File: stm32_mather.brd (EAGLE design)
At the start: 100 x 80 mm, 56 parts

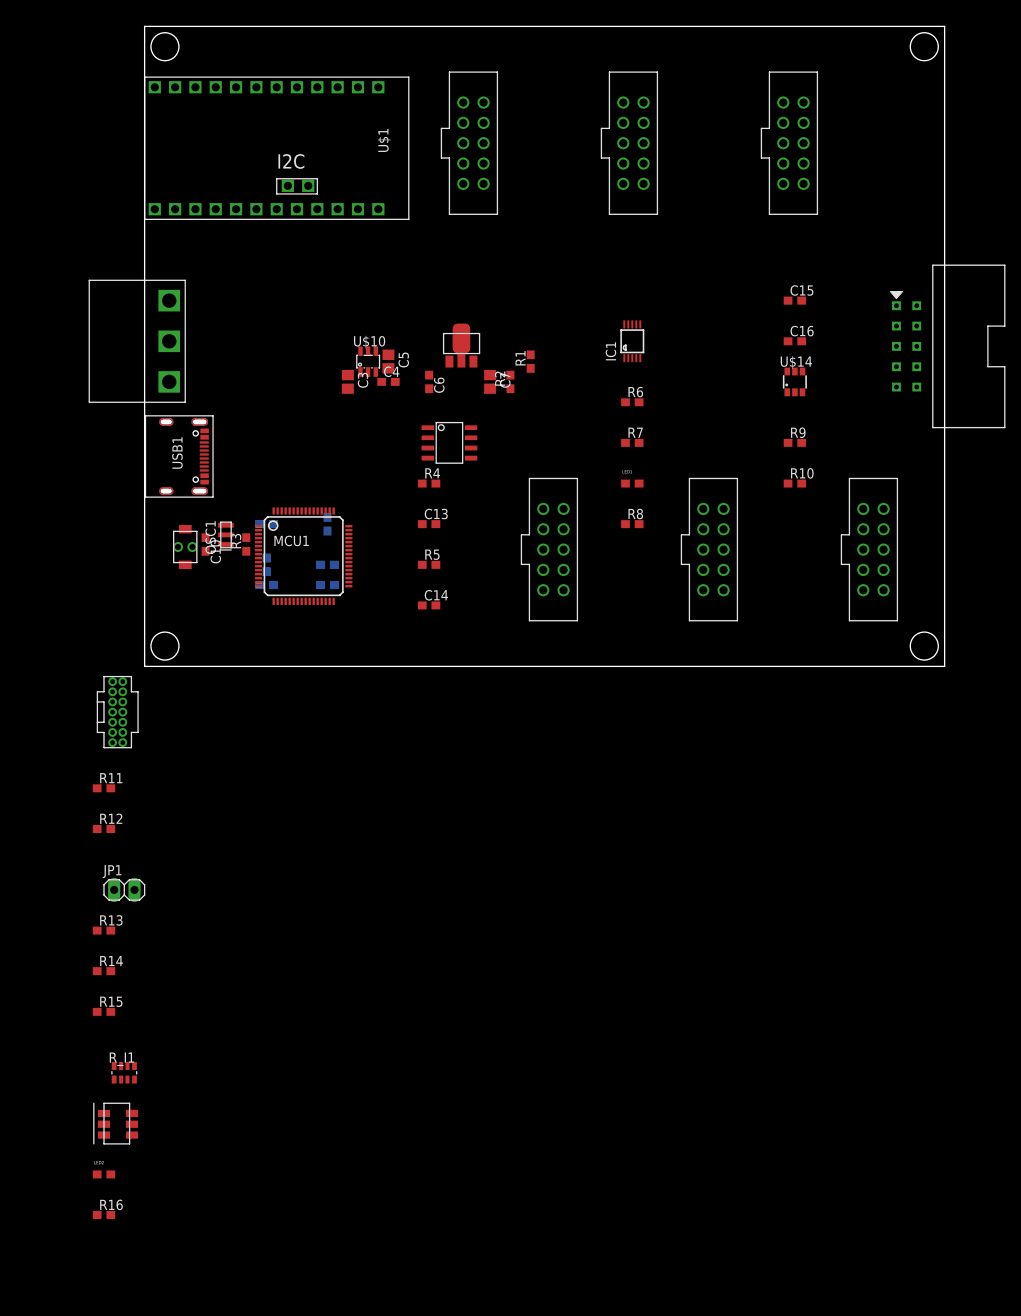
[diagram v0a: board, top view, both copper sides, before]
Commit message: デバッガを組み込む方式に変更 3.3vのリニアレギュレータを単純化
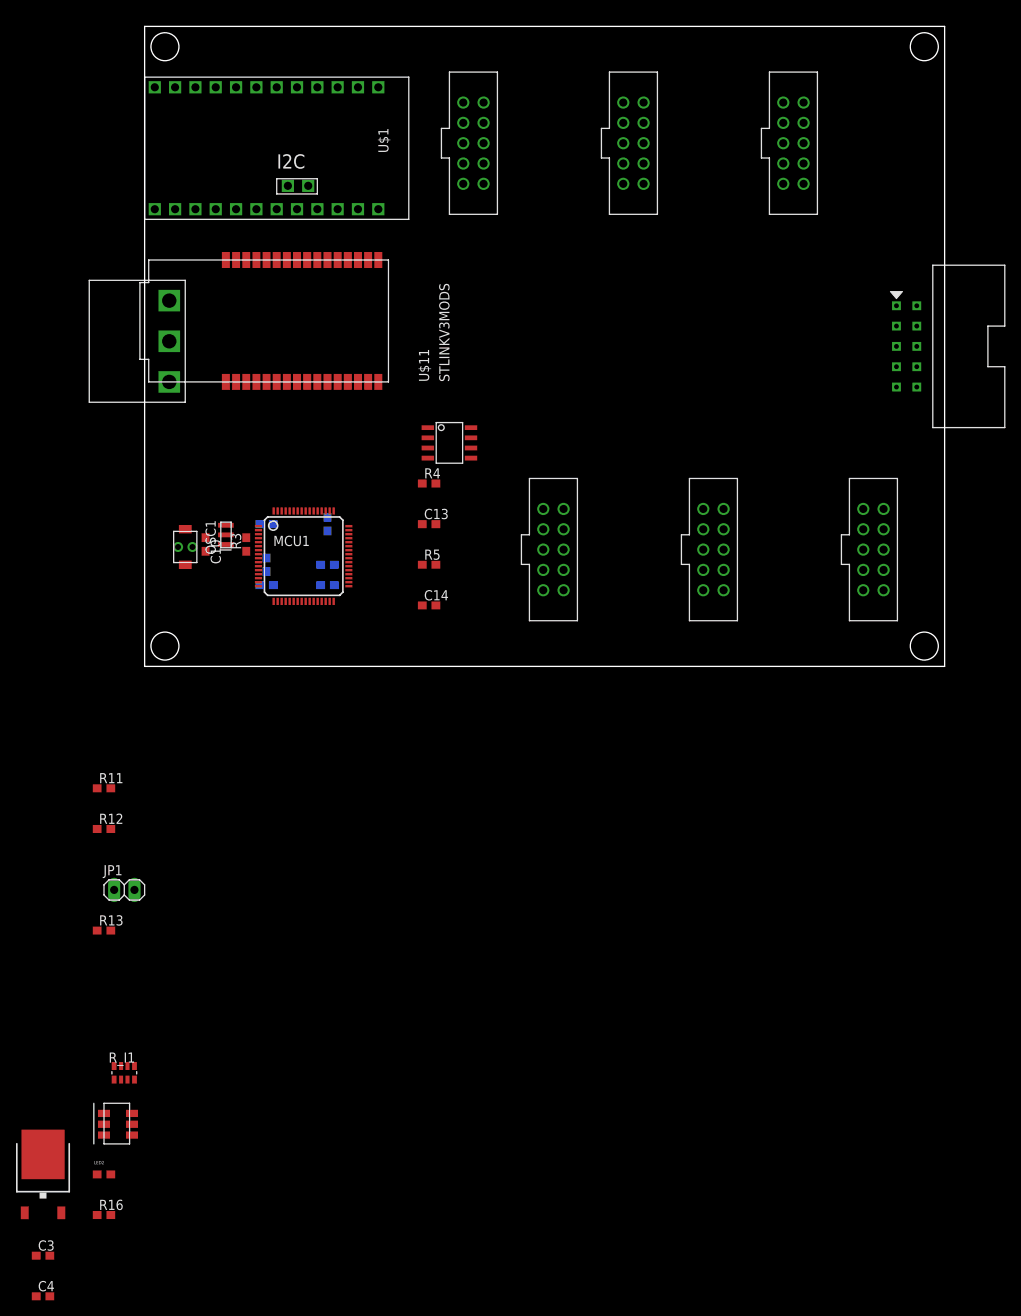
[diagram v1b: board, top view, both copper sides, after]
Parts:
- removed C15: 0.1u, rcl:C1608
- removed C16: (no value), rcl:C1608
- removed C5: 4.7u, rcl:C2012
- removed C6: 470p, rcl:C1608
- removed C7: 10u, rcl:C2012
- removed IC1: (no value), user_ic:MSOP10
- removed LED1: (no value), user_leds:1608
- removed R1: 33k, user_rcl:1608
- removed R10, R14, R15, R9: 10k, user_rcl:1608
- removed R2: 20k, user_rcl:1608
- removed R6, R7: 5.1k, user_rcl:1608
- removed R8: 1k, user_rcl:1608
- removed U$14: FDC6305, user_tr_fet_igbt:SSOT6
- removed U$22: BOX14P, user_conector:CON_HEDA14P_1.27
- removed USB1: (no value), user_conector:USB_TYPE_C
- C3: value 0.22u -> 1u; device rcl:C2012 -> rcl:C1608
- C4: value 0.1u -> 2.2u
- U$10: value NJM11100 -> NJM2845; device user_ic:SOT23-6 -> user_ic:TO252
- U$11: value 2SC5964 -> STLINKV3MODS; device user_tr_fet_igbt:PCP -> user_ic:STLINKV3MODS
- moved C4 122.2 mm to (-12.7, -78.7)
- moved C3 115.7 mm to (-12.7, -73.7), turned to 0 degrees
- moved U$10 109.4 mm to (-12.7, -63.5)
- moved U$11 8.03 mm to (30.5, 35.6), turned to 90 degrees
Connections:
- removed net N$1: C6.2, R1.1, R2.2, U$10.5
- removed net N$17: IC1.1, USB1.A6, USB1.B6
- removed net N$18: IC1.2, USB1.A7, USB1.B7
- removed net N$2: C4.1, U$10.3
- removed net N$20: R7.2, USB1.A5
- removed net N$21: R6.2, USB1.B5
- removed net N$22: IC1.6, R8.1
- removed net N$23: LED1.A, R8.2
- removed net N$24: C15.1, IC1.10
- removed net N$25: IC1.4, IC1.5
- removed net N$26: IC1.8, R10.2, U$14.2
- removed net N$28: IC1.9, R9.1, U$14.5
- removed net N$3: C5.1, C6.1, U$10.4, U$11.1
- removed net USART1_RX: MCU1.59, R14.1, U$14.4
- removed net USART1_TX: MCU1.58, R15.1, U$14.6
- net GND: now also U$10.PIN2, U$11.24, U$11.26, U$11.27, U$11.29, U$11.5, U$11.8; no longer C15.2, C16.2, C5.2, C7.2, IC1.3, LED1.K, R2.1, R6.1, R7.1, U$10.2, U$22.11, U$22.5, U$22.7, USB1.A1_B12, USB1.B1_A12
- net JTCK: now also U$11.13; no longer U$22.6
- net JTDI: now also U$11.28; no longer U$22.10
- net JTDO: now also U$11.6; no longer U$22.8
- net JTMS: now also U$11.4; no longer U$22.4
- net NRST: now also U$11.31; no longer U$22.12
- net RX: now also U$11.15; no longer U$22.13
- net TX: now also U$11.12; no longer U$22.14
- net V3.3: now also C4.1, U$10.PIN3, U$11.30; no longer C7.1, R1.2, R14.2, R15.2, U$11.3, U$22.3
- net V5: now also U$10.PIN1; no longer C16.1, IC1.7, R10.1, R9.2, U$10.1, U$10.6, U$11.2, U$11.2@2, U$14.1, U$14.3, USB1.A4_B9, USB1.B4_A9

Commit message: 基板図の設計完了
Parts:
- R_I1: value (none) -> 1k
- moved C4 119.6 mm to (11.8, 38.3), turned to 270 degrees
- moved R16 118.6 mm to (29.5, 44.8)
- moved R13 115.2 mm to (83.7, 40.4), flipped to the bottom, turned to 270 degrees
- moved C3 113.6 mm to (6.72, 38.3), turned to 270 degrees
- moved JP1 111.3 mm to (87.6, 37.3), turned to 180 degrees
- moved LED2 110.3 mm to (44.4, 35.1)
- moved U$10 101.7 mm to (9.26, 35.8), flipped to the bottom, turned to 180 degrees
- moved U$15 100.1 mm to (46.1, 30.2), turned to 180 degrees
- moved R_I1 94.5 mm to (39.6, 33.8), turned to 90 degrees
- moved R12 74.6 mm to (26.2, 47.4), turned to 180 degrees
- moved R11 66.9 mm to (25.3, 44.3), turned to 180 degrees
- moved C14 31.9 mm to (42.7, 38.7), flipped to the bottom, turned to 90 degrees
- moved R5 30.4 mm to (41.7, 42.4), turned to 180 degrees
- moved U$11 27.9 mm to (30.5, 7.62)
- moved C9 24.6 mm to (31.3, 33.3), turned to 90 degrees
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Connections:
- removed net N$13: C12.2, MCU1.18
- removed net N$14: C12.1, MCU1.19
- removed net N$15: C11.1, MCU1.47
- removed net N$16: C11.2, MCU1.48
- removed net N$30: C10.2, C2.2, MCU1.13, U$12.P$1
- removed net N$5: C9.1, MCU1.32
- removed net N$7: C2.1, MCU1.12
- removed net N$8: C8.1, MCU1.64
- removed net N$9: C8.2, MCU1.63
- net GND: now also C10.2, C11.1, C12.2, C2.1, C8.2, MCU1.12, MCU1.18, MCU1.47, MCU1.63, U$1.23, U$1.4, U$12.P$1, U$15.B_K, U$15.G_K, U$15.R_K; no longer U$15.B_A, U$15.G_A, U$15.R_A
- net N$10: now also U$15.R_A; no longer U$15.R_K
- net N$29: now also U$15.G_A; no longer U$15.G_K
- net N$31: now also U$15.B_A; no longer U$15.B_K
- net V3.3: now also C11.2, C12.1, C2.2, C8.1, C9.1, MCU1.13, MCU1.19, MCU1.32, MCU1.48, MCU1.64
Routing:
- net CANH: track 0.00 -> 238.1 mm, vias 0 -> 1
- net CANL: track 0.00 -> 225.0 mm, vias 0 -> 1
- net V3.3: track 0.00 -> 89.0 mm, vias 0 -> 9
- net JTDO: track 0.00 -> 56.6 mm, vias 0 -> 2
- net JTMS: track 0.00 -> 49.2 mm, vias 0 -> 2
- net JTCK: track 0.00 -> 43.2 mm, vias 0 -> 4
- net JTDI: track 0.00 -> 40.4 mm, vias 0 -> 2
- net V5: track 0.00 -> 34.1 mm, vias 0 -> 51
- net GND: track 0.00 -> 30.8 mm, vias 0 -> 440
- net TX: track 0.00 -> 26.3 mm, vias 0 -> 2
- net RX: track 0.00 -> 26.2 mm, vias 0 -> 2
- net NRST: track 0.00 -> 23.7 mm, vias 0 -> 3
- net SDA: track 0.00 -> 20.6 mm
- net SCL: track 0.00 -> 19.9 mm
- net CANRX: track 0.00 -> 6.49 mm
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- added copper zone on layer 1, net GND
- added copper zone on layer 16, net GND
- added copper zone on layer 1, net V12
- added copper zone on layer 16, net V12
- added copper zone on layer 1, net V5
- added copper zone on layer 16, net V5
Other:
- board text added: "0.hayate"
- board text added: "KRP"
- board text added: "STM32F446RE/RC_CanBus_MatherBord"

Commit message: drcを通した
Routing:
- net V3.3: track 89.0 -> 99.9 mm, vias 9 -> 10
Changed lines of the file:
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@@
 <via x="6.72" y="39.15" extent="1-16" drill="0.35"/>
 <via x="38.94" y="37.965" extent="1-16" drill="0.35"/>
-<wire x1="40.425" y1="37.965" x2="40.6" y2="37.79" width="0.1524" layer="16"/>
 <wire x1="40.6" y1="37.79" x2="39.115" y2="37.79" width="0.3048" layer="16"/>
 <wire x1="39.115" y1="37.79" x2="38.94" y2="37.965" width="0.3048" layer="16"/>
@@
 <wire x1="44.615" y1="39.51" x2="44.86" y2="39.51" width="0.3048" layer="1"/>
 <via x="44.86" y="39.51" extent="1-16" drill="0.35"/>
-<wire x1="83.72" y1="41.21" x2="83.92" y2="41.2396" width="0.508" layer="16"/>
 <wire x1="44.86" y1="39.51" x2="50.8" y2="39.51" width="0.508" layer="16"/>
 <wire x1="50.8" y1="39.51" x2="55.88" y2="39.51" width="0.508" layer="16"/>
@@
 <via x="23.68" y="36.13" extent="1-16" drill="0.35"/>
 <via x="23.31" y="32.72" extent="1-16" drill="0.35"/>
-<wire x1="24.25" y1="30.99" x2="24.2286" y2="31.0114" width="0.1524" layer="1"/>
 <via x="31.3" y="34.15" extent="1-16" drill="0.35"/>
 <via x="29.16" y="34.13" extent="1-16" drill="0.35"/>
@@
 <via x="25.01" y="32.72" extent="1-16" drill="0.35"/>
 <via x="23.68" y="34.43" extent="1-16" drill="0.35"/>
-<wire x1="21.85" y1="40.39" x2="21.9" y2="40.44" width="0.1524" layer="1"/>
 <via x="23.21" y="40.44" extent="1-16" drill="0.35"/>
 <via x="31.38" y="40.89" extent="1-16" drill="0.35"/>
@@
 <wire x1="42.1098" y1="35.6598" x2="43.145" y2="36.695" width="0.3048" layer="1"/>
 <wire x1="39.3348" y1="35.6598" x2="42.1098" y2="35.6598" width="0.3048" layer="1"/>
-<wire x1="26.15" y1="44.34" x2="27.07" y2="47.36" width="0" layer="19" extent="1-1"/>
-<wire x1="23.75" y1="42.29" x2="26.15" y2="44.34" width="0" layer="19" extent="1-1"/>
+<wire x1="26.15" y1="44.34" x2="27.07" y2="45.26" width="0.1524" layer="1"/>
+<wire x1="27.07" y1="45.26" x2="27.07" y2="45.72" width="0.1524" layer="1"/>
+<wire x1="27.07" y1="45.72" x2="27.07" y2="47.36" width="0.1524" layer="1"/>
+<wire x1="27.07" y1="45.72" x2="25.806" y2="45.72" width="0.1524" layer="1"/>
+<via x="25.806" y="45.72" extent="1-16" drill="0.35"/>
+<wire x1="25.806" y1="45.72" x2="23.21" y2="43.124" width="0.1524" layer="16"/>
+<wire x1="23.21" y1="43.124" x2="23.21" y2="40.44" width="0.1524" layer="16"/>
 </signal>
 <signal name="N$4">
@@
 <wire x1="86.32" y1="37.31" x2="85.92" y2="37.31" width="0.508" layer="16"/>
 <wire x1="83.72" y1="39.51" x2="85.92" y2="37.31" width="0.508" layer="16"/>
-<wire x1="86.32" y1="37.31" x2="86.33" y2="37.3" width="0" layer="19" extent="16-16"/>
+<wire x1="86.33" y1="37.3" x2="86.32" y2="37.31" width="0.1524" layer="16"/>
 </signal>
 <signal name="N$10">
